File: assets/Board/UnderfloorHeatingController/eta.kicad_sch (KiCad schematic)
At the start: 3 parts, among them J5 Screw_Terminal_01x02, U4 AQY214EH

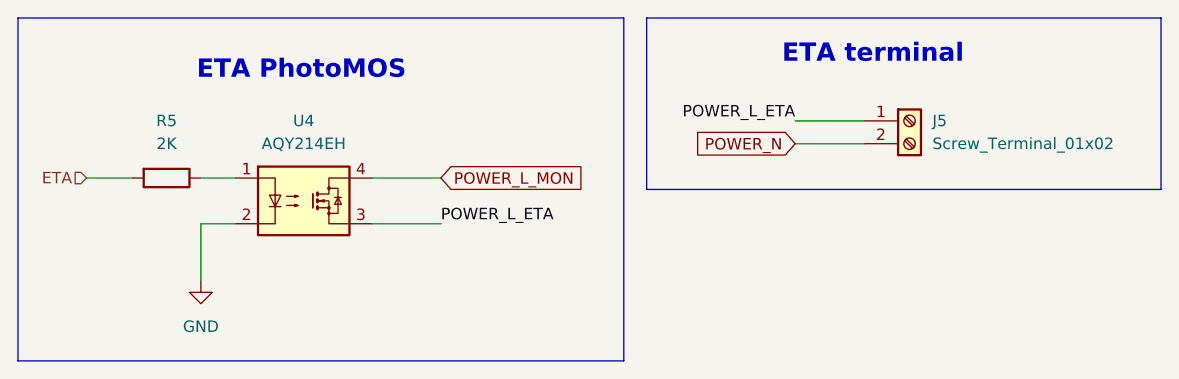
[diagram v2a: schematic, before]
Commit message: Changed resistor size.
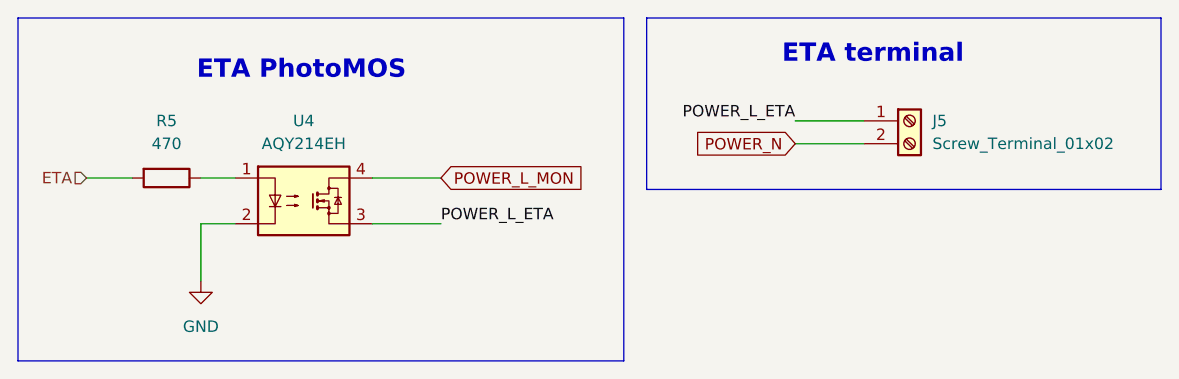
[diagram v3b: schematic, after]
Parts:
- R5: value 2K -> 470
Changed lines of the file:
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@@
 			)
 		)
-		(property "Value" "2K"
+		(property "Value" "470"
 			(at 30.48 27.94 90)
 			(effects
